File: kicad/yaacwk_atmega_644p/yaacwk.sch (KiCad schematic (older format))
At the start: 47 parts, among them IC2 TLP627-2, J1 Ext PWR, J2 TX Key, J3 TX PTT, SW1 SW_PUSH, SW2 SW_PUSH, SW3 SW_PUSH, SW4 SW_PUSH, SW5 SW_PUSH

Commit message: Updated YAACWK Kicad to allign with latest pin settings for AtMega 644p variant
   moved ps2_keyboard_clock to pin2 (pin3 on AtMega 644p is not an interrupt capable pin!)
   moved paddle_left to pin3
   added cw decoder indicator LED on pin30
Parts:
- added D4: LED, ~, symbol LED-RESCUE-yaacwk
- added R9: 220Ω, ~, symbol R-RESCUE-yaacwk
- gave numbers to parts that had none: 1
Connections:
- wire segments 194 -> 195
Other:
- moved on the sheet: J?

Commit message: fix eechema, cw_decored reenabled and speed pot now is working
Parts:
- SpeedPot1: value 100k -> 10k
- gave numbers to parts that had none: 1
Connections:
- wire segments 195 -> 153
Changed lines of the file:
@@
 P 4200 6600
 F 0 "SpeedPot1" H 4200 6500 50  0000 C CNN
-F 1 "100k" H 4200 6600 50  0000 C CNN
+F 1 "10k" H 4200 6600 50  0000 C CNN
 F 2 "~" H 4200 6600 60  0000 C CNN
 F 3 "~" H 4200 6600 60  0000 C CNN
@@
 $EndComp
 $Comp
-L POT-RESCUE-yaacwk SpeedPot?
+L POT-RESCUE-yaacwk LightPot
 U 1 1 57261201
 P 7550 3750
-F 0 "SpeedPot?" H 7550 3650 50  0000 C CNN
+F 0 "LightPot" H 7550 3650 50  0000 C CNN
 F 1 "10k" H 7550 3750 50  0000 C CNN
 F 2 "~" H 7550 3750 60  0000 C CNN
@@
 Connection ~ 5200 6800
 Wire Wire Line
-	5200 6600 5200 6800
+	5200 6800 5200 6600
 Connection ~ 4600 6800
 Connection ~ 4850 6800
 Wire Wire Line
-	4850 6600 4850 6800
+	4850 6800 4850 6600
 Connection ~ 3900 5600
 Wire Wire Line
@@
 Connection ~ 4850 5600
 Wire Wire Line
-	600  5600 3900 5600
-Wire Wire Line
-	3900 5600 4850 5600
+	600  5600 4850 5600
 Wire Wire Line
 	1600 5800 1600 6200
@@
 	8250 4100 9200 4100
 Wire Wire Line
-	8050 5300 8050 4800
-Wire Wire Line
-	8050 4800 8050 4300
-Wire Wire Line
-	8050 4300 8050 3900
-Wire Wire Line
-	8050 3900 8050 3750
+	8050 3750 8050 5400
 Connection ~ 5400 800
 Wire Wire Line
-	5400 850  5400 800
+	5400 800  5400 850
 Wire Wire Line
 	8050 4300 9200 4300
@@
 Connection ~ 5400 1350
 Wire Wire Line
-	5200 1350 5400 1350
-Wire Wire Line
-	5400 1350 5550 1350
+	5200 1350 5550 1350
 Wire Wire Line
 	9400 1800 10350 1800
@@
 	4050 2700 4750 2700
 Wire Wire Line
-	5600 2000 5600 4600
-Wire Wire Line
-	5600 4600 5600 5700
+	5600 2000 5600 5700
 Wire Wire Line
 	7600 2000 7950 2000
 Connection ~ 4850 800
 Wire Wire Line
-	5400 1850 5400 5300
-Wire Wire Line
-	5400 5300 5400 6800
-Wire Wire Line
-	5400 6800 5400 6900
-Wire Wire Line
-	4600 6150 4600 6600
-Wire Wire Line
-	4600 6600 4600 6800
+	5400 1850 5400 6900
+Wire Wire Line
+	4600 6800 4600 6150
 Wire Wire Line
 	3000 5200 3000 5300
@@
 	1650 1300 1650 1400
 Wire Wire Line
-	1450 1400 1650 1400
-Wire Wire Line
-	1650 1400 1850 1400
+	1450 1400 1850 1400
 Connection ~ 1850 1900
 Wire Wire Line
@@
 	1500 1900 1450 1900
 Wire Wire Line
-	1450 1700 1450 1900
-Wire Wire Line
-	1450 1900 1450 2300
+	1450 1700 1450 2300
 Wire Wire Line
 	1450 2300 2050 2300
 Wire Wire Line
-	1800 1900 1850 1900
-Wire Wire Line
-	1850 1900 2050 1900
+	1800 1900 2050 1900
 Wire Wire Line
 	9250 3700 9250 3300
 Wire Wire Line
-	1100 6800 1600 6800
-Wire Wire Line
-	1600 6800 2250 6800
-Wire Wire Line
-	2250 6800 2850 6800
-Wire Wire Line
-	2850 6800 3500 6800
-Wire Wire Line
-	3500 6800 4600 6800
-Wire Wire Line
-	4600 6800 4850 6800
-Wire Wire Line
-	4850 6800 5200 6800
-Wire Wire Line
-	5200 6800 5400 6800
-Wire Wire Line
-	5400 6800 5600 6800
-Wire Wire Line
-	5600 6800 5900 6800
+	1100 6800 5900 6800
 Wire Wire Line
 	4450 6600 4600 6600
@@
 	4600 650  8700 650
 Wire Wire Line
-	1100 5450 1100 5800
-Wire Wire Line
-	1100 5800 1100 6200
-Wire Wire Line
-	2100 5300 3000 5300
-Wire Wire Line
-	3000 5300 3100 5300
-Wire Wire Line
-	3100 5300 5400 5300
-Wire Wire Line
-	5400 5300 8050 5300
+	1100 5450 1100 6200
+Wire Wire Line
+	2100 5300 8050 5300
 Wire Wire Line
 	3100 5300 3100 5200
 Connection ~ 3200 800
 Wire Wire Line
-	3200 1200 3200 800
+	3200 800  3200 1200
 Wire Wire Line
 	2900 800  2900 1200
 Wire Wire Line
-	1250 800  2900 800
-Wire Wire Line
-	2900 800  3200 800
-Wire Wire Line
-	3200 800  4850 800
-Wire Wire Line
-	4850 800  5000 800
-Wire Wire Line
-	5000 800  5400 800
-Wire Wire Line
-	5400 800  9050 800
+	1250 800  9050 800
 Wire Wire Line
 	4200 1500 4050 1500
 Wire Wire Line
-	4200 1500 4200 6150
-Wire Wire Line
-	4200 6150 4200 6450
+	4200 1500 4200 6450
 Wire Wire Line
 	3900 5600 3900 6600
@@
 	6800 2550 6800 2800
 Wire Wire Line
-	4650 3200 8950 3200
-Wire Wire Line
-	8950 3200 9450 3200
+	4650 3200 9450 3200
 Wire Wire Line
 	10400 650  9300 650
@@
 	7600 2550 7950 2550
 Wire Wire Line
-	8850 2300 9000 2300
-Wire Wire Line
-	9000 2300 9400 2300
-Wire Wire Line
-	9400 2300 9800 2300
-Wire Wire Line
-	8850 1900 9000 1900
-Wire Wire Line
-	9000 1900 9250 1900
-Wire Wire Line
-	8400 3700 8650 3700
-Wire Wire Line
-	8650 3700 8950 3700
-Wire Wire Line
-	8950 3700 9250 3700
+	8850 2300 9800 2300
+Wire Wire Line
+	8850 1900 9250 1900
+Wire Wire Line
+	8400 3700 9250 3700
 Wire Wire Line
 	10500 1600 10500 1300
@@
 Connection ~ 9400 2300
 Wire Wire Line
-	8800 2850 9000 2850
-Wire Wire Line
-	9000 2850 9400 2850
+	8800 2850 9400 2850
 Wire Wire Line
 	8800 2750 8800 2850
@@
 	2200 5000 2200 4500
 Wire Wire Line
-	4850 800  4850 5600
-Wire Wire Line
-	4850 5600 4850 5700
+	4850 800  4850 5700
 Wire Wire Line
 	9800 2550 9950 2550
 Wire Wire Line
-	9800 2100 9800 2300
-Wire Wire Line
-	9800 2300 9800 2550
-Wire Wire Line
-	8800 2450 9000 2450
-Wire Wire Line
-	9000 2450 9950 2450
-Wire Wire Line
-	7700 2200 7700 2750
-Wire Wire Line
-	7700 2750 7700 2850
+	9800 2100 9800 2550
+Wire Wire Line
+	8800 2450 9950 2450
+Wire Wire Line
+	7700 2200 7700 2850
 Connection ~ 7700 2750
 Wire Wire Line
-	4750 3000 8650 3000
-Wire Wire Line
-	8650 3000 9450 3000
+	4750 3000 9450 3000
 Wire Wire Line
 	2350 5800 2250 5800
 Wire Wire Line
-	7300 2750 7700 2750
-Wire Wire Line
-	7700 2750 7950 2750
-Wire Wire Line
-	5200 2200 5200 4500
-Wire Wire Line
-	5200 4500 5200 5700
+	7300 2750 7950 2750
+Wire Wire Line
+	5200 2200 5200 5700
 Wire Wire Line
 	6450 6250 6250 6250
@@
 Wire Wire Line
 	5900 2100 4050 2100
+Wire Wire Line
+	8050 5400 9200 5400
+Connection ~ 8050 5300
+Wire Wire Line
+	9200 5300 8150 5300
+Wire Wire Line
+	8150 5300 8150 4000
+Connection ~ 8150 4000
 $EndSCHEMATC

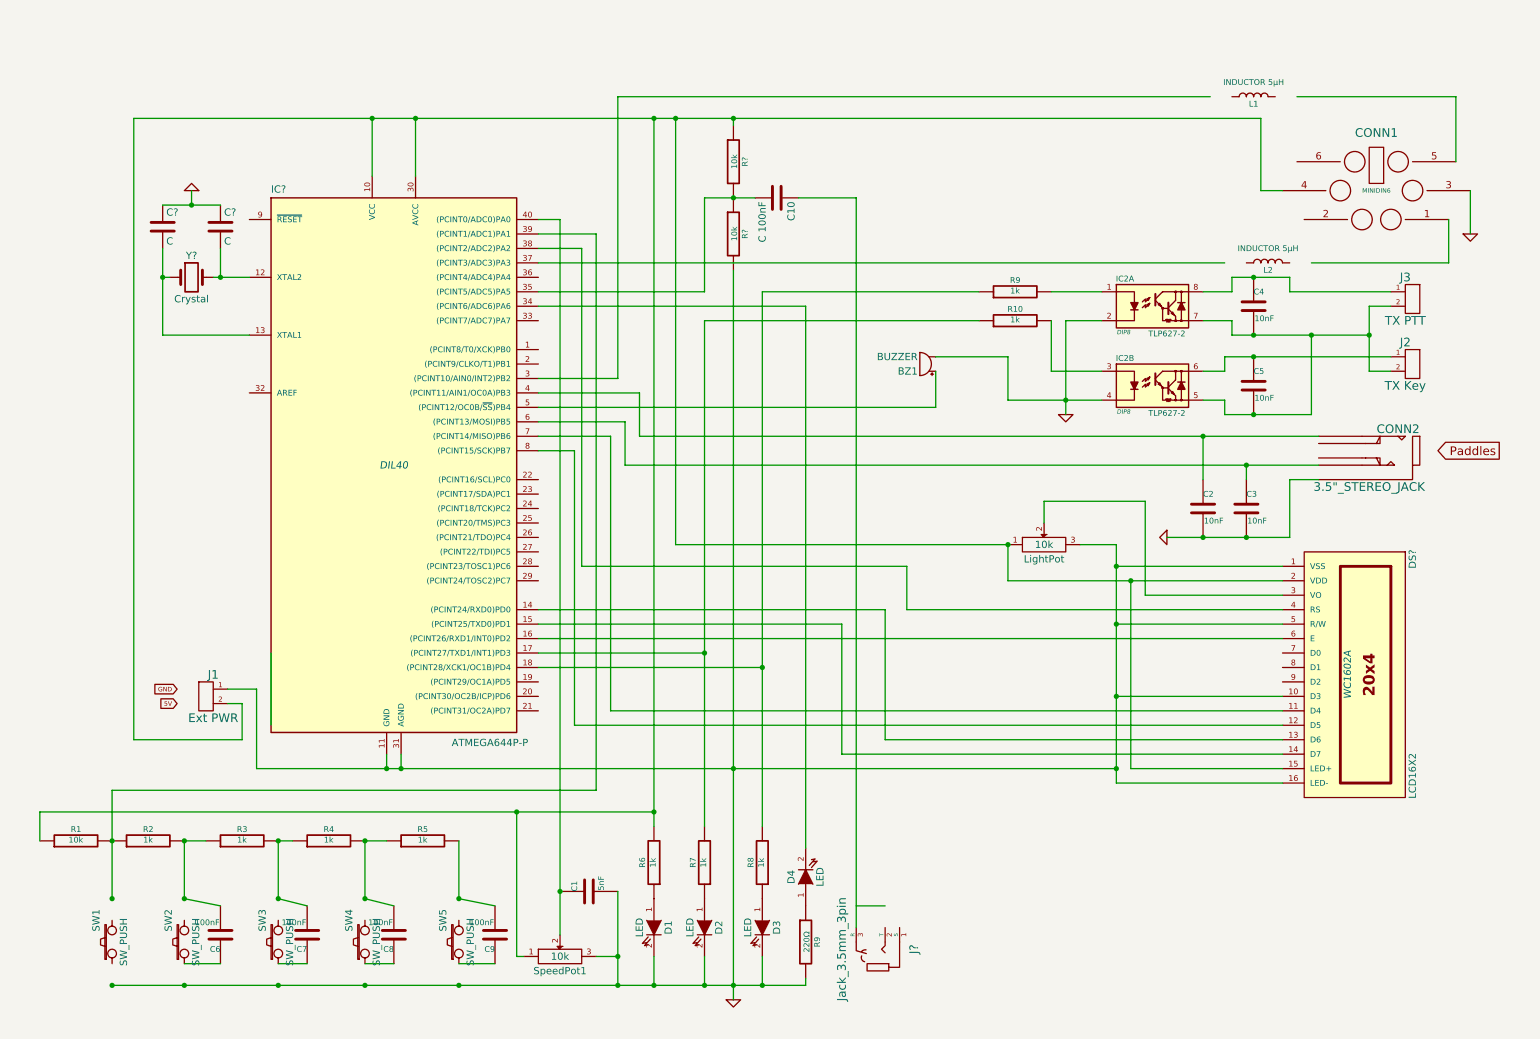
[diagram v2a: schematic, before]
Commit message: fix yaawck eeschema for display, to reflect the current src code
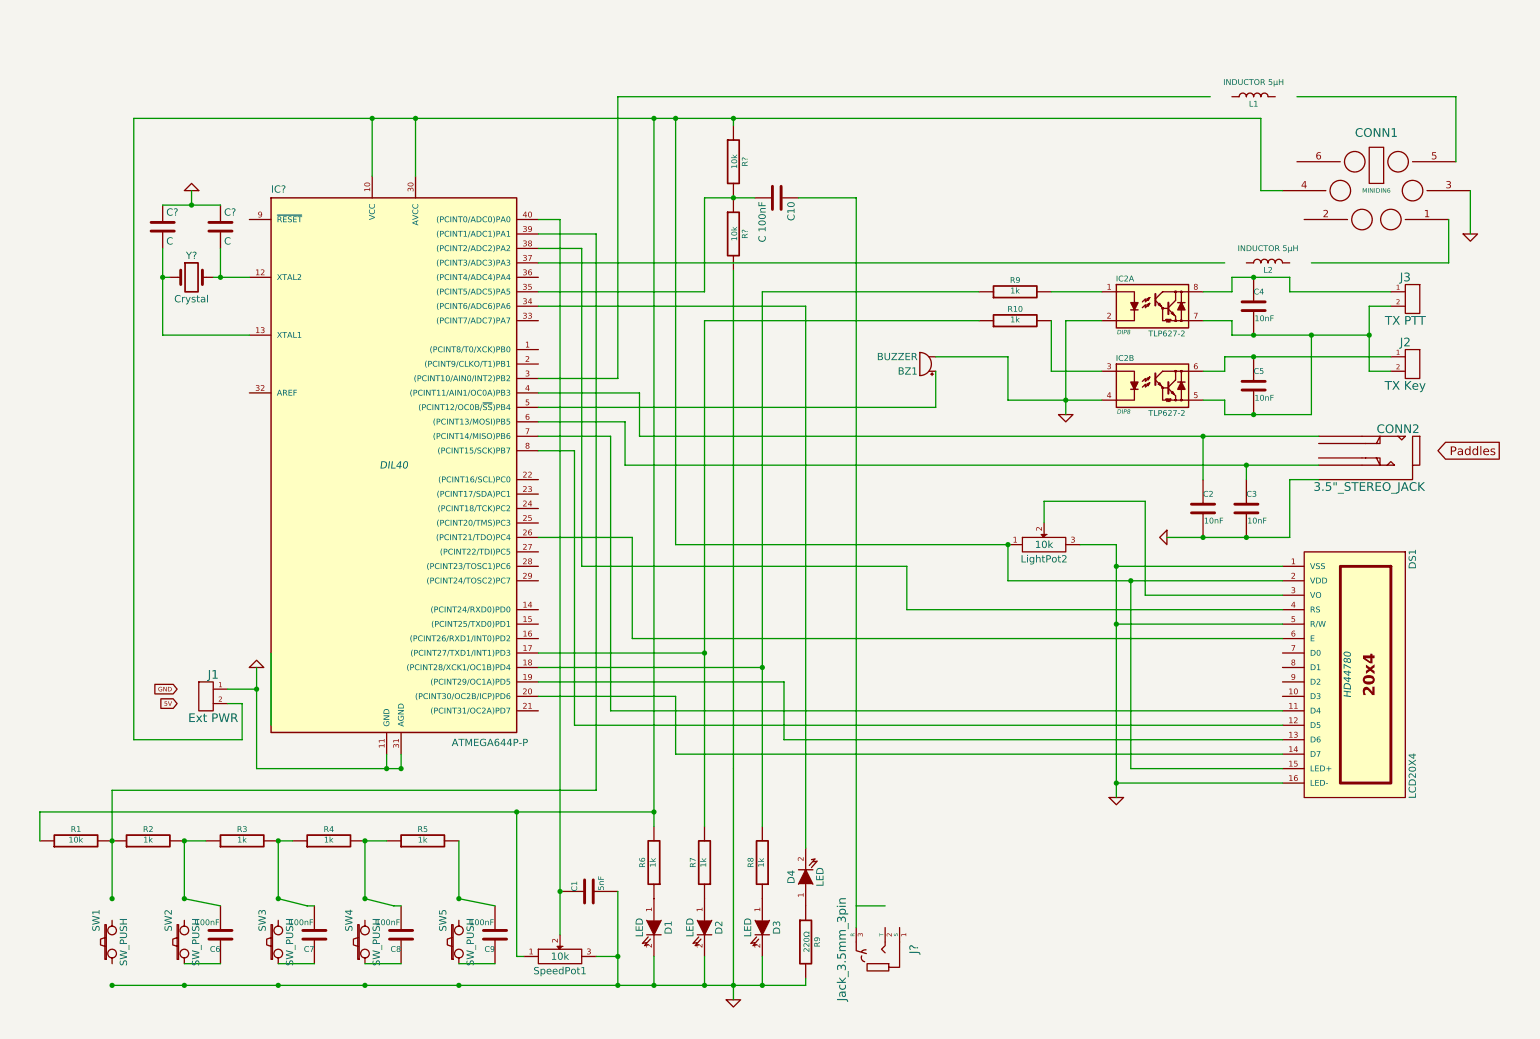
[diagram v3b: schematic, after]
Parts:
- DS1: renamed from DS?; value LCD16X2 -> LCD20X4; footprint WC1602A -> HD44780
- renumbered LightPot to LightPot2
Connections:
- wire segments 153 -> 201
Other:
- moved on the sheet: C7, C8

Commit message: yaacwk, eeschema cleanup, ps2 pinout fixed, uart ttl and new power input added
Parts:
- removed CONN1: MINIDIN6, symbol miniDIN6
- removed CONN2: 3.5\"_STEREO_JACK, symbol 3.5"_STEREO_JACK
- removed J2: TX Key, symbol HEADER_2
- removed J3: TX PTT, symbol HEADER_2
- removed J?: Jack_3.5mm_3pin, symbol Jack_3.5mm_3pin
- added C13: 50mF, Capacitors_THT:CP_Radial_D5.0mm_P2.50mm, symbol CP1
- added C14: 350mF, Capacitors_THT:CP_Radial_D8.0mm_P2.50mm, symbol CP1
- added D5, D6: D_ALT, Diodes_THT:D_A-405_P7.62mm_Horizontal, symbol D_ALT
- added J2: AUDIO_IN, custom_kicad_footprints:PJ320E_3.5mm_4_conductors_audio_plug, symbol PJ320E_3.5mm_4_conductors_audio_plug
- added J3: TX_PTT, Pin_Headers:Pin_Header_Straight_1x02_Pitch2.54mm, symbol CONN_01X02
- added J4: TX_KEY, Pin_Headers:Pin_Header_Straight_1x02_Pitch2.54mm, symbol CONN_01X02
- added J5: PADDLES, Pin_Headers:Pin_Header_Straight_1x03_Pitch2.54mm, symbol CONN_01X03
- added J6: TTL_SERIAL, Pin_Headers:Pin_Header_Straight_1x06_Pitch2.54mm, symbol HEADER_6
- added PS2CONN1: Mini-DIN_6pins_ver4, mini_din6:Mini_din6, symbol Mini-DIN_6pins_ver4
- added SW6: SW_PUSH, Pin_Headers:Pin_Header_Straight_1x02_Pitch2.54mm, symbol SW_PUSH-RESCUE-yaacwk
- added U1: LM7805, mojes-kicad-footprints:78XX, symbol LM7805
- BZ1: footprint (none) -> Buzzers_Beepers:Buzzer_12x9.5RM7.6
- C1, C2, C3, C4, C5, C6, C7, C8, C9: footprint ~ -> Capacitors_ThroughHole:C_Disc_D7.5_P5
- C10, C11: renamed from C?; value C -> 22 pF; footprint (none) -> Capacitors_ThroughHole:C_Disc_D7.5_P5
- C12: renamed from C10; value C 100nF -> 100nF; footprint (none) -> Capacitors_ThroughHole:C_Disc_D7.5_P5
- D1, D2, D3: footprint ~ -> LEDs:LED_D3.0mm
- D4: footprint ~ -> LEDs:LED_D5.0mm
- DS1: footprint HD44780 -> Pin_Headers:Pin_Header_Straight_2x08_Pitch2.54mm
- IC1: renamed from IC?; footprint DIL40 -> Housings_DIP:DIP-40_W15.24mm
- IC2: footprint DIP8 -> Housings_DIP:DIP-8_W7.62mm
- J1: value Ext PWR -> EXT_PWR; footprint (none) -> Connect:AK300-2
- L1, L2: footprint ~ -> Inductors_THT:L_Axial_L7.0mm_D3.3mm_P10.16mm_Horizontal_Fastron_MICC; symbol INDUCTOR -> INDUCTOR-RESCUE-yaacwk
- LCDPot2: renamed from LightPot2; value 10k -> 10kOhm; footprint ~ -> w_pth_resistors:trimmer_piher_pt6xv
- R1: value 10k -> 10kOhm; footprint ~ -> Resistors_THT:R_Axial_DIN0207_L6.3mm_D2.5mm_P7.62mm_Horizontal
- R10: renamed from R9; value 1k -> 1kOhm; footprint ~ -> Resistors_THT:R_Axial_DIN0207_L6.3mm_D2.5mm_P7.62mm_Horizontal
- R11: renamed from R10; value 1k -> 1kOhm; footprint ~ -> Resistors_THT:R_Axial_DIN0207_L6.3mm_D2.5mm_P7.62mm_Horizontal
- R12, R13: renamed from R?; value 10k -> 10kOhm; footprint ~ -> Resistors_THT:R_Axial_DIN0207_L6.3mm_D2.5mm_P7.62mm_Horizontal
- R2, R3, R4, R5, R6, R7, R8: value 1k -> 1kOhm; footprint ~ -> Resistors_THT:R_Axial_DIN0207_L6.3mm_D2.5mm_P7.62mm_Horizontal
- R9: value 220Ω -> 220 Ohm; footprint ~ -> Resistors_THT:R_Axial_DIN0207_L6.3mm_D2.5mm_P7.62mm_Horizontal
- SW1, SW2, SW3, SW4, SW5: footprint ~ -> Pin_Headers:Pin_Header_Straight_1x02_Pitch2.54mm; symbol SW_PUSH -> SW_PUSH-RESCUE-yaacwk
- SpeedPot1: value 10k -> 10kOhm; footprint ~ -> Potentiometers:Potentiometer_Trimmer_Suntan_TSR-3386C_Vertical
- Y1: renamed from Y?; value Crystal -> Crystal 16 Mhz; footprint (none) -> Crystals:Crystal_HC49-U_Vertical
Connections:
- net labels added: +5V
- net labels removed: 5V, Paddles
- wire segments 201 -> 171
- no-connect marks 0 -> 24
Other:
- moved on the sheet: BZ1, C1, C10, C11, C12, C2, C3, C4, C5, C6, C7, C8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

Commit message: yaacwk pcb v1.1_RC updated eechema
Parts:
- removed C13: 50mF, Capacitors_THT:CP_Radial_D5.0mm_P2.50mm, symbol CP1
- removed J2: AUDIO_IN, custom_kicad_footprints:PJ320E_3.5mm_4_conductors_audio_plug, symbol PJ320E_3.5mm_4_conductors_audio_plug
- added C13, C15: 220nF, Capacitors_ThroughHole:C_Disc_D7.5_P5, symbol C
- added C16: 330uF, Capacitors_THT:CP_Radial_D8.0mm_P3.80mm, symbol CP1
- added C17, C18, C19: 100nF, Capacitors_ThroughHole:C_Disc_D7.5_P5, symbol C
- added J2: AUDIO_IN, PJ320A:PJ320A_3.5mm_4_conductors_audio_plug, symbol PJ320A_3.5mm_4_conductors_audio_plug
- added J7: HEADER_6, Pin_Headers:Pin_Header_Straight_1x06_Pitch2.54mm, symbol HEADER_6
- added J8: HEADER_11, Pin_Headers:Pin_Header_Straight_1x11_Pitch2.54mm, symbol HEADER_11
- added J9: PWR_SEL, Pin_Headers:Pin_Header_Straight_1x03_Pitch2.54mm, symbol HEADER_3
- added R14, R15, R16: 1kOhm, Resistors_THT:R_Axial_DIN0207_L6.3mm_D2.5mm_P7.62mm_Horizontal, symbol R
- added SW7, SW8, SW9: SW_PUSH, Pin_Headers:Pin_Header_Straight_1x02_Pitch2.54mm, symbol SW_PUSH
- added U2: LM2937, mojes-kicad-footprints:78XX, symbol LM7805
- C14: value 350mF -> 330uF; footprint Capacitors_THT:CP_Radial_D8.0mm_P2.50mm -> Capacitors_THT:CP_Radial_D8.0mm_P3.80mm
- C2, C3, C4, C5, C6, C7, C8, C9: symbol C-RESCUE-yaacwk -> C
- D1, D2, D3: symbol LED-RESCUE-yaacwk -> LED
- D4: footprint LEDs:LED_D5.0mm -> LEDs:LED_D3.0mm; symbol LED-RESCUE-yaacwk -> LED
- DS1: footprint Pin_Headers:Pin_Header_Straight_2x08_Pitch2.54mm -> Pin_Headers:Pin_Header_Straight_1x16_Pitch2.54mm
- IC2: symbol TLP627-2-RESCUE-yaacwk -> TLP627-2
- J1: footprint Connect:AK300-2 -> Connectors:BARREL_JACK; symbol HEADER_2 -> HEADER_3
- L1, L2: symbol INDUCTOR-RESCUE-yaacwk -> INDUCTOR
- LCDPot2: footprint w_pth_resistors:trimmer_piher_pt6xv -> Potentiometers:Potentiometer_Trimmer_ACP_CA9h5_Vertical_Px5.0mm_Py5.0mm; symbol POT-RESCUE-yaacwk -> POT
- PS2CONN1: footprint mini_din6:Mini_din6 -> mini_din6New:Mini_din6
- R1, R12, R13, R2, R3, R4, R5, R9: symbol R-RESCUE-yaacwk -> R
- R6, R7, R8: value 1kOhm -> 470 Ohm; symbol R-RESCUE-yaacwk -> R
- SW1, SW2, SW3, SW4, SW5, SW6: symbol SW_PUSH-RESCUE-yaacwk -> SW_PUSH
- SpeedPot1: footprint Potentiometers:Potentiometer_Trimmer_Suntan_TSR-3386C_Vertical -> Potentiometers:Potentiometer_Alps_RK097_Single_Vertical; symbol POT-RESCUE-yaacwk -> POT
- Y1: value Crystal 16 Mhz -> Crystal 16 MHz
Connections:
- wire segments 171 -> 249
- no-connect marks 24 -> 11
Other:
- moved on the sheet: C1, C12, C7, C8, C9, D1, D2, D3, D4, D5, DS1, IC2A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
